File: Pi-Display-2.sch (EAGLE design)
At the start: 13 parts, among them IC1 MCP2515-I/SO, IC2 MCP2562-E/SN, J1 RJ45 CAN.Bus, Q1 16MHz, U1 TSR 2-2450

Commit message: Layouts angepasst
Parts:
- added C7: 10µF/25V, rcl:C-EUC1206
- C6: value 22µF 50V Low-ESR -> 10µF/25V; device rcl:CPOL-EUE2-5 -> rcl:C-EUC1206
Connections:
- net +24V: now also C6.1, C7.1; no longer C6.+
- net GND: now also C6.2, C7.2; no longer C6.-
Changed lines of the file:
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@@
 <setting verticaltext="up"/>
 </settings>
-<grid distance="0.1" unitdist="inch" unit="inch" style="lines" multiple="1" display="yes" altdistance="0.01" altunitdist="inch" altunit="inch"/>
+<grid distance="0.1" unitdist="inch" unit="inch" style="lines" multiple="1" display="no" altdistance="0.01" altunitdist="inch" altunit="inch"/>
 <layers>
 <layer number="1" name="Top" color="4" fill="1" visible="no" active="no"/>
@@
 <class number="0" name="default" width="0" drill="0">
 </class>
+<class number="1" name="24V" width="0.8128" drill="0">
+<clearance class="1" value="0.4064"/>
+</class>
 </classes>
 <parts>
@@
 <part name="C5" library="rcl" deviceset="C-EU" device="C1206" value="22pF"/>
 <part name="U1" library="TSR" deviceset="TSR2-*" device="" technology="2450" value="TSR 2-2450"/>
-<part name="C6" library="rcl" deviceset="CPOL-EU" device="E2-5" value="22µF 50V Low-ESR"/>
+<part name="C7" library="rcl" deviceset="C-EU" device="C1206" value="10µF/25V"/>
+<part name="C6" library="rcl" deviceset="C-EU" device="C1206" value="10µF/25V"/>
 </parts>
 <sheets>
@@
 <instance part="C5" gate="G$1" x="147.32" y="114.3" rot="R90"/>
 <instance part="U1" gate="U1" x="48.26" y="154.94"/>
-<instance part="C6" gate="G$1" x="25.4" y="149.86"/>
+<instance part="C7" gate="G$1" x="33.02" y="149.86"/>
+<instance part="C6" gate="G$1" x="15.24" y="149.86"/>
 </instances>
 <busses>
@@
 <wire x1="48.26" y1="147.32" x2="48.26" y2="142.24" width="0.1524" layer="91"/>
 <label x="63.5" y="142.24" size="1.778" layer="95"/>
-<pinref part="C6" gate="G$1" pin="-"/>
 <wire x1="48.26" y1="142.24" x2="63.5" y2="142.24" width="0.1524" layer="91"/>
-<wire x1="25.4" y1="144.78" x2="25.4" y2="142.24" width="0.1524" layer="91"/>
-<wire x1="25.4" y1="142.24" x2="48.26" y2="142.24" width="0.1524" layer="91"/>
+<wire x1="15.24" y1="144.78" x2="15.24" y2="142.24" width="0.1524" layer="91"/>
+<wire x1="15.24" y1="142.24" x2="33.02" y2="142.24" width="0.1524" layer="91"/>
 <junction x="48.26" y="142.24"/>
+<pinref part="C6" gate="G$1" pin="2"/>
+<pinref part="C7" gate="G$1" pin="2"/>
+<wire x1="33.02" y1="142.24" x2="48.26" y2="142.24" width="0.1524" layer="91"/>
+<wire x1="33.02" y1="144.78" x2="33.02" y2="142.24" width="0.1524" layer="91"/>
+<junction x="33.02" y="142.24"/>
 </segment>
 </net>
@@
 </segment>
 </net>
-<net name="+24V" class="0">
+<net name="+24V" class="1">
 <segment>
 <pinref part="J1" gate="G$1" pin="4"/>
@@
 <segment>
 <pinref part="U1" gate="U1" pin="VI"/>
-<wire x1="38.1" y1="154.94" x2="25.4" y2="154.94" width="0.1524" layer="91"/>
-<label x="17.78" y="154.94" size="1.778" layer="95" rot="MR0"/>
-<pinref part="C6" gate="G$1" pin="+"/>
-<wire x1="25.4" y1="154.94" x2="17.78" y2="154.94" width="0.1524" layer="91"/>
-<wire x1="25.4" y1="152.4" x2="25.4" y2="154.94" width="0.1524" layer="91"/>
-<junction x="25.4" y="154.94"/>
-</segment>
-</net>
+<wire x1="38.1" y1="154.94" x2="33.02" y2="154.94" width="0.1524" layer="91"/>
+<label x="10.16" y="154.94" size="1.778" layer="95" rot="MR0"/>
+<wire x1="33.02" y1="154.94" x2="15.24" y2="154.94" width="0.1524" layer="91"/>
+<wire x1="15.24" y1="154.94" x2="10.16" y2="154.94" width="0.1524" layer="91"/>
+<wire x1="15.24" y1="152.4" x2="15.24" y2="154.94" width="0.1524" layer="91"/>
+<junction x="15.24" y="154.94"/>
+<pinref part="C6" gate="G$1" pin="1"/>
+<pinref part="C7" gate="G$1" pin="1"/>
+<wire x1="33.02" y1="152.4" x2="33.02" y2="154.94" width="0.1524" layer="91"/>
+<junction x="33.02" y="154.94"/>
+</segment>
+</net>

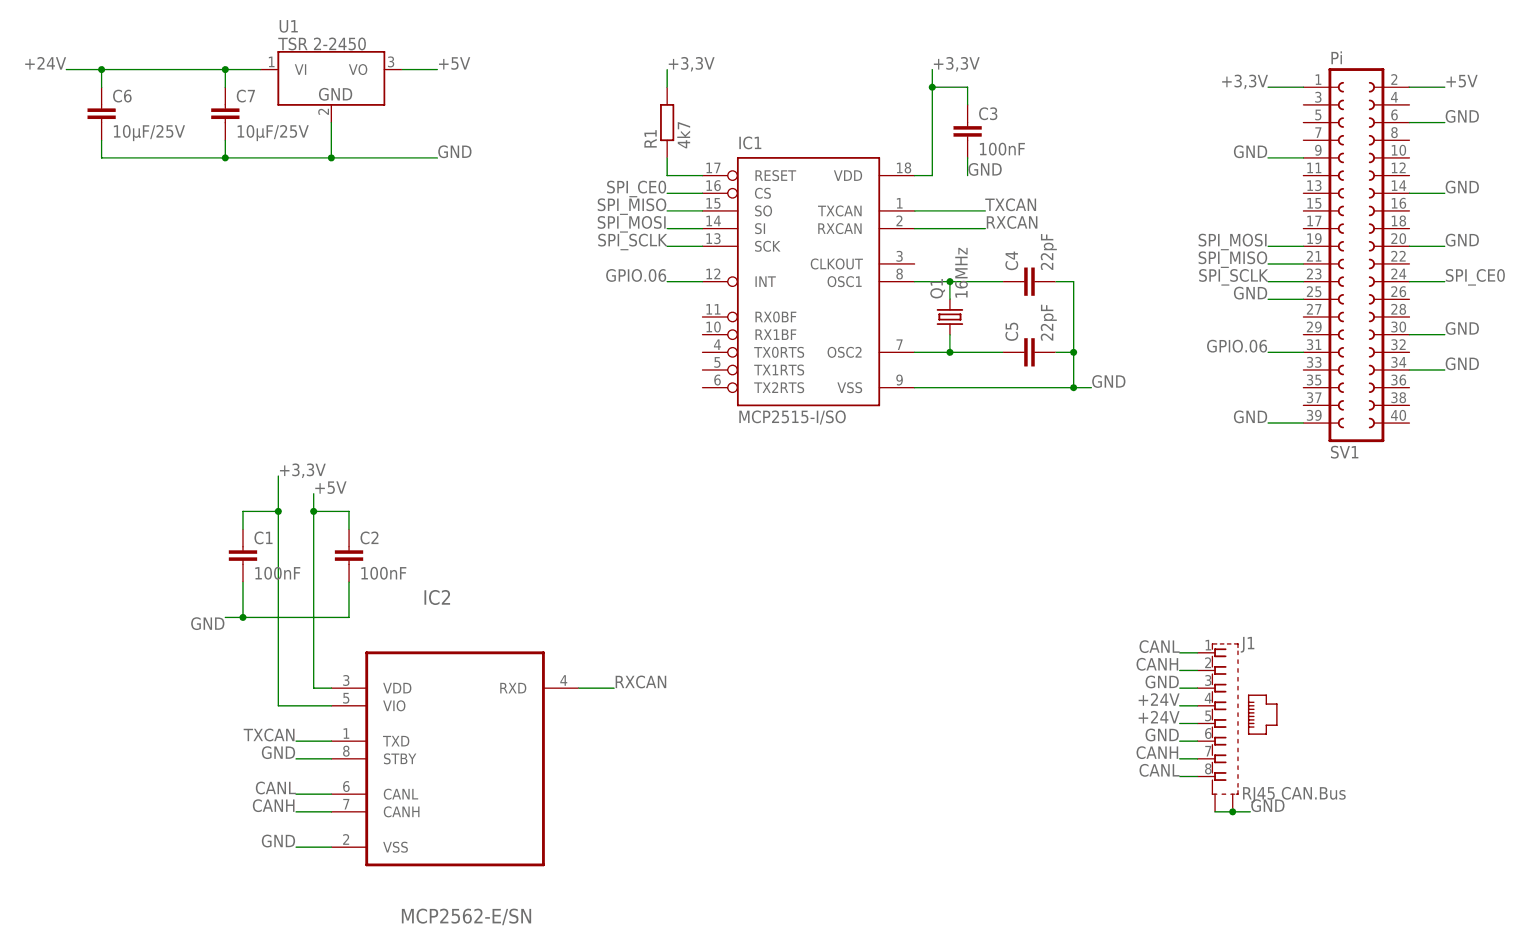
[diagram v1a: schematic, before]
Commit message: CAN-Bus Beadboard-Adapter, Layouts angepasst
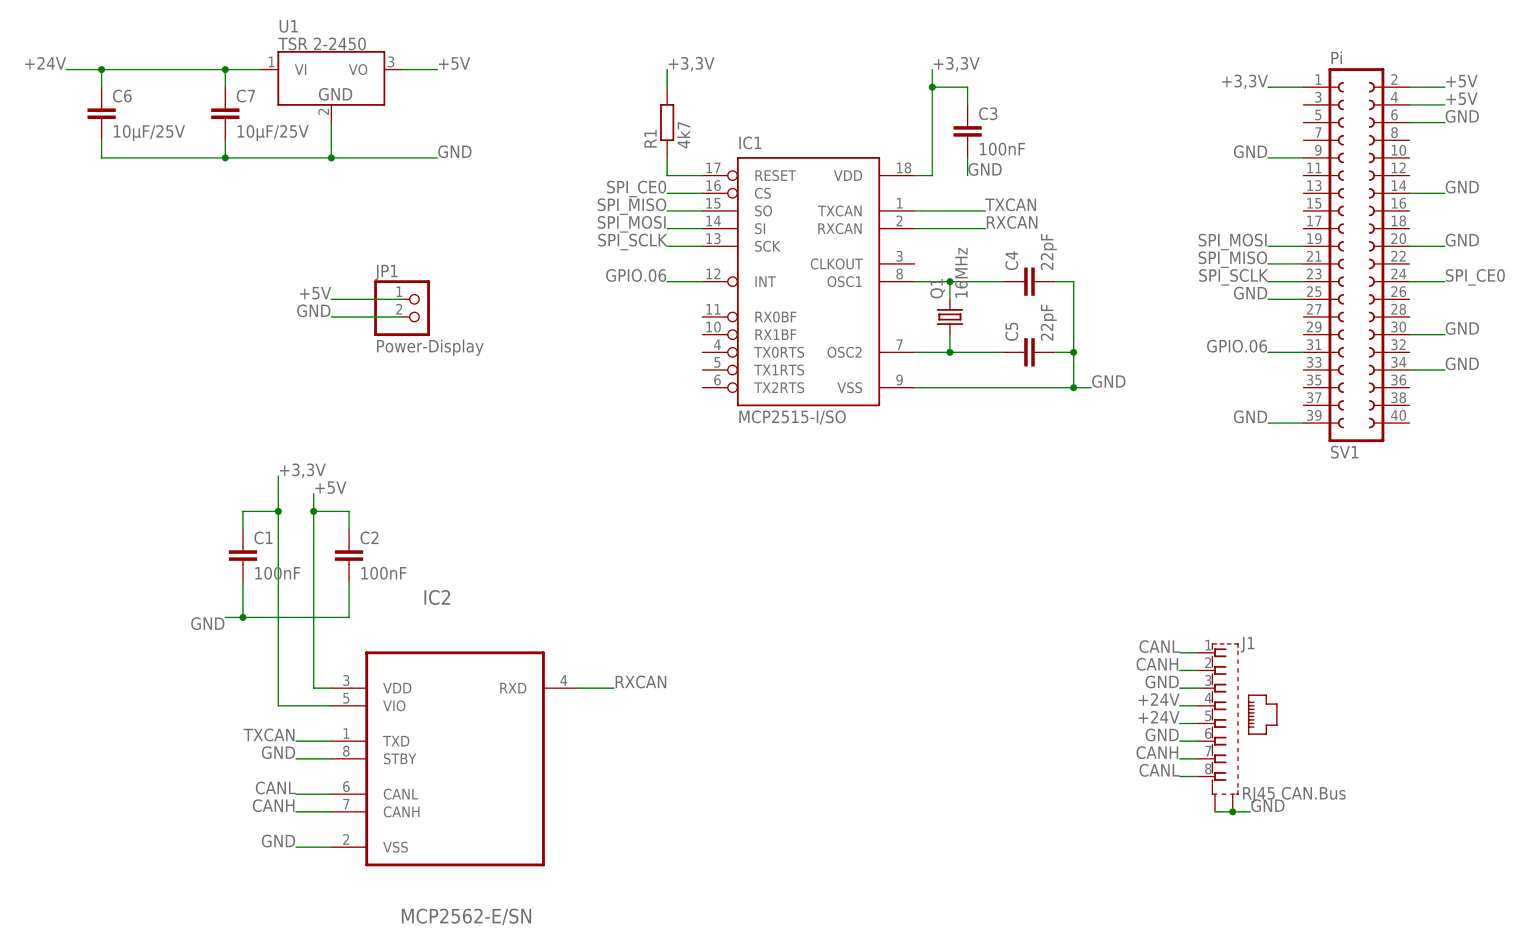
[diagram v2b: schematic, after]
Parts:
- added JP1: Power-Display, pinhead:PINHD-1X2/90
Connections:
- net +5V: now also JP1.1, SV1.4
- net GND: now also JP1.2
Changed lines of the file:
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@@
 <part name="C7" library="rcl" deviceset="C-EU" device="C1206" value="10µF/25V"/>
 <part name="C6" library="rcl" deviceset="C-EU" device="C1206" value="10µF/25V"/>
+<part name="JP1" library="pinhead" deviceset="PINHD-1X2" device="/90" value="Power-Display"/>
 </parts>
 <sheets>
@@
 <instance part="C7" gate="G$1" x="33.02" y="149.86"/>
 <instance part="C6" gate="G$1" x="15.24" y="149.86"/>
+<instance part="JP1" gate="G$1" x="60.96" y="119.38"/>
 </instances>
 <busses>
@@
 <wire x1="58.42" y1="154.94" x2="63.5" y2="154.94" width="0.1524" layer="91"/>
 <label x="63.5" y="154.94" size="1.778" layer="95"/>
+</segment>
+<segment>
+<pinref part="JP1" gate="G$1" pin="1"/>
+<wire x1="58.42" y1="121.92" x2="48.26" y2="121.92" width="0.1524" layer="91"/>
+<label x="48.26" y="121.92" size="1.778" layer="95" rot="MR0"/>
+</segment>
+<segment>
+<pinref part="SV1" gate="G$1" pin="4"/>
+<wire x1="203.2" y1="149.86" x2="208.28" y2="149.86" width="0.1524" layer="91"/>
+<label x="208.28" y="149.86" size="1.778" layer="95"/>
 </segment>
 </net>
@@
 <junction x="33.02" y="142.24"/>
 </segment>
-</net>
+<segment>
+<pinref part="JP1" gate="G$1" pin="2"/>
+<wire x1="58.42" y1="119.38" x2="48.26" y2="119.38" width="0.1524" layer="91"/>
+<label x="48.26" y="119.38" size="1.778" layer="95" rot="MR0"/>
+</segment>
+</net>
